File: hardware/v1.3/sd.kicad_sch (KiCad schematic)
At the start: 3 parts, among them J6 Micro_SD_Card_Det2, U1 ECP5-CABGA256

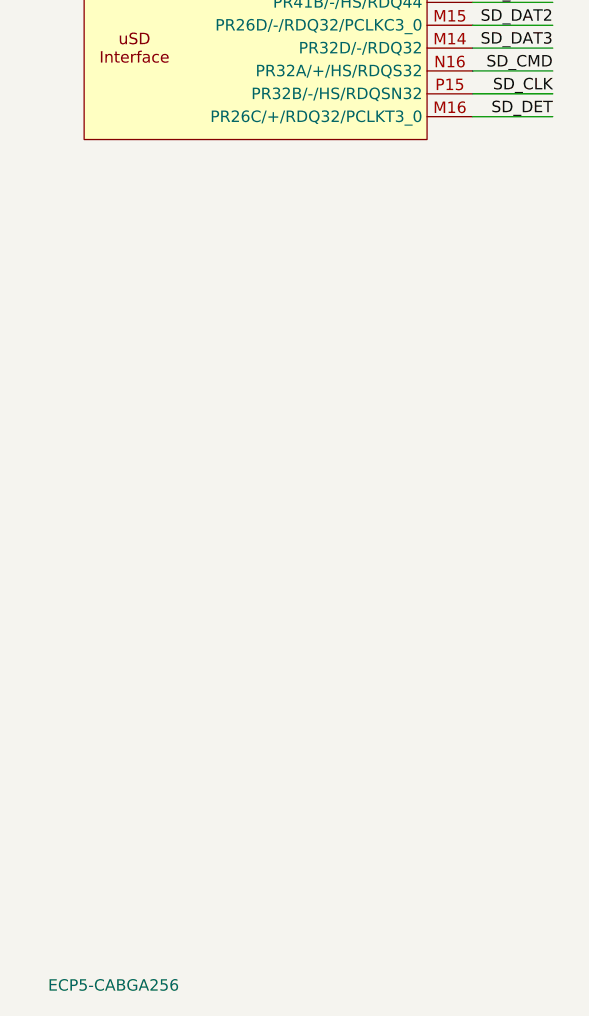
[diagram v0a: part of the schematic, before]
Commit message: Refine README
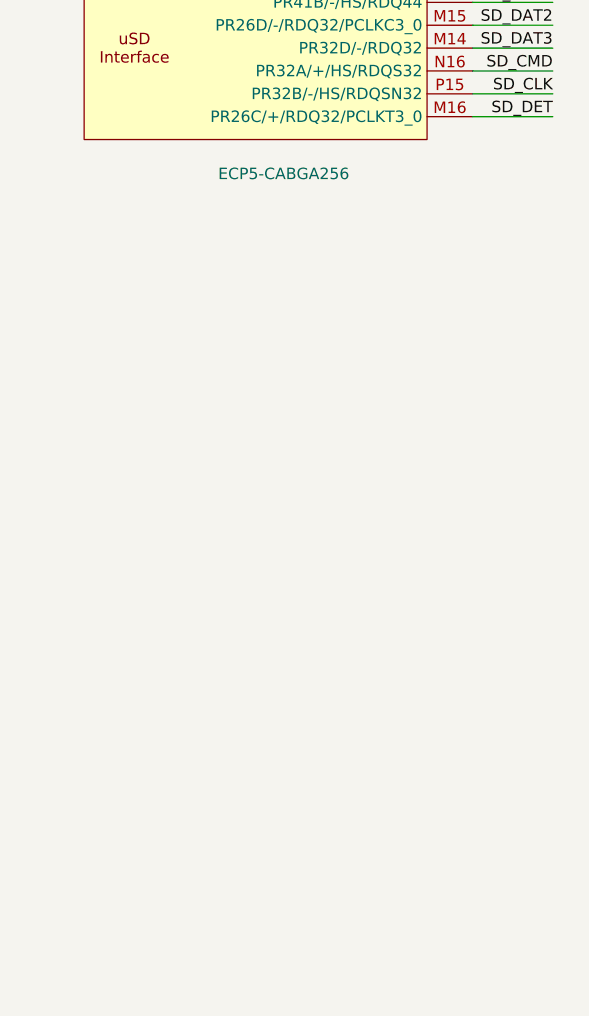
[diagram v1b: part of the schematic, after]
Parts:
- C47: LCSC Link (none) -> https://lcsc.com/product-detail/Multilayer-Ceramic-Capacito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; Manufactuer Part Number (none) -> CL10A106KP8NNNC
- J6: LCSC Link (none) -> https://lcsc.com/product-detail/SD-Card-Memory-Card-Connect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; Manufactuer Part Number (none) -> TF-008
- U1: LCSC Link (none) -> https://lcsc.com/product-detail/Programmable-Logic-Device-C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; LCSC Part # (none) -> C1521614; Manufactuer Part Number (none) -> LFE5U-25F-6BG256C

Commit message: Update files
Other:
- moved on the sheet: C47, J6
